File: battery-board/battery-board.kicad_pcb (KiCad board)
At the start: 2 copper layers, 101.6 x 14 mm, 6 parts, among them J1 Conn_01x02_Male, J2 Conn_01x03, J3 Screw_Terminal_01x01, SW1 RESET

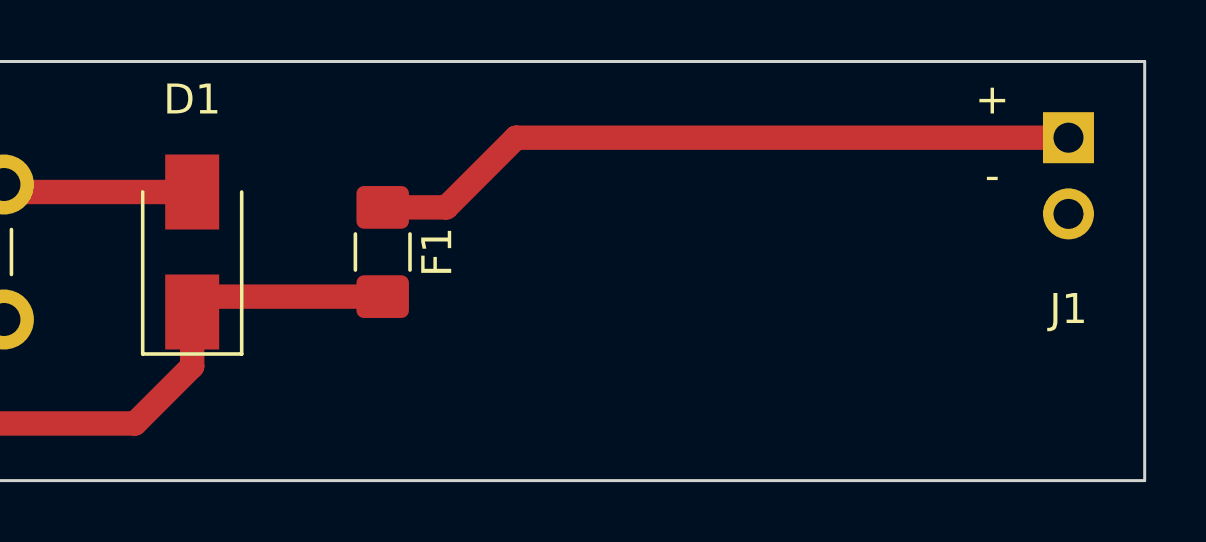
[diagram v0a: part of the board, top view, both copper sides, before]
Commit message: updated to a different fuse
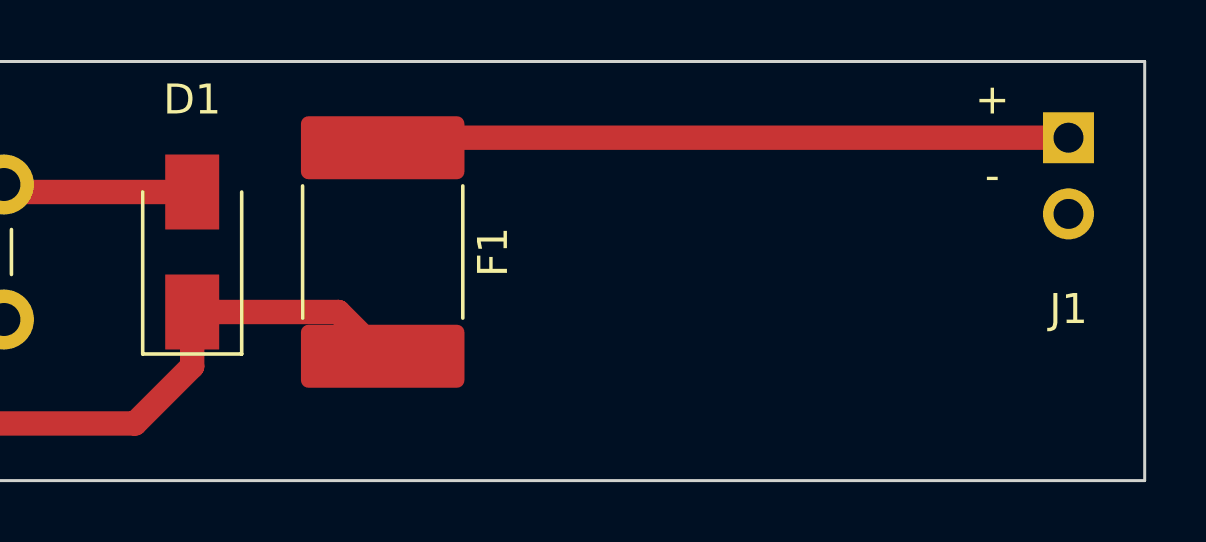
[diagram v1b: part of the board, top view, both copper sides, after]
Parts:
- F1: footprint Fuse:Fuse_1206_3216Metric_Pad1.42x1.75mm_HandSolder -> project:Fuse_2920_7451Metric_Pad2.10x5.45mm_HandSolder
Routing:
- net /VBB: track 23.8 -> 23.0 mm
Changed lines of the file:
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@@
 		)
 	)
-	(footprint "Fuse:Fuse_1206_3216Metric_Pad1.42x1.75mm_HandSolder"
+	(footprint "project:Fuse_2920_7451Metric_Pad2.10x5.45mm_HandSolder"
 		(layer "F.Cu")
 		(at 165.1 101.6 -90)
-		(descr "Fuse SMD 1206 (3216 Metric), square (rectangular) end terminal, IPC_7351 nominal with elongated pad for handsoldering. (Body size source: http://www.tortai-tech.com/upload/download/2011102023233369053.pdf), generated with kicad-footprint-generator")
+		(descr "Fuse SMD 2920 (7451 Metric), square (rectangular) end terminal, IPC_7351 nominal with elongated pad for handsoldering. (Body size from: http://www.megastar.com/products/fusetronic/polyswitch/PDF/smd2920.pdf), generated with kicad-footprint-generator")
 		(tags "fuse handsolder")
 		(property "Reference" "F1"
-			(at 0 -1.82 270)
+			(at 0 -3.68 270)
 			(layer "F.SilkS")
 			(effects
@@
 		)
 		(property "Value" "0.5A"
-			(at 0 1.82 270)
+			(at 0 3.68 270)
 			(layer "F.Fab")
 			(effects
@@
 		(attr smd)
 		(fp_line
-			(start -0.602064 0.91)
-			(end 0.602064 0.91)
+			(start -2.203752 2.67)
+			(end 2.203752 2.67)
 			(stroke
 				(width 0.12)
@@
 		)
 		(fp_line
-			(start -0.602064 -0.91)
-			(end 0.602064 -0.91)
+			(start -2.203752 -2.67)
+			(end 2.203752 -2.67)
 			(stroke
 				(width 0.12)
@@
 		)
 		(fp_line
-			(start -2.45 1.12)
-			(end -2.45 -1.12)
+			(start -4.78 2.98)
+			(end -4.78 -2.98)
 			(stroke
 				(width 0.05)
@@
 		)
 		(fp_line
-			(start 2.45 1.12)
-			(end -2.45 1.12)
+			(start 4.78 2.98)
+			(end -4.78 2.98)
 			(stroke
 				(width 0.05)
@@
 		)
 		(fp_line
-			(start -2.45 -1.12)
-			(end 2.45 -1.12)
+			(start -4.78 -2.98)
+			(end 4.78 -2.98)
 			(stroke
 				(width 0.05)
@@
 		)
 		(fp_line
-			(start 2.45 -1.12)
-			(end 2.45 1.12)
+			(start 4.78 -2.98)
+			(end 4.78 2.98)
 			(stroke
 				(width 0.05)
@@
 		)
 		(fp_line
-			(start -1.6 0.8)
-			(end -1.6 -0.8)
-			(stroke
-				(width 0.1)
-				(type solid)
-			)
-			(layer "F.Fab")
-		)
-		(fp_line
-			(start 1.6 0.8)
-			(end -1.6 0.8)
-			(stroke
-				(width 0.1)
-				(type solid)
-			)
-			(layer "F.Fab")
-		)
-		(fp_line
-			(start -1.6 -0.8)
-			(end 1.6 -0.8)
-			(stroke
-				(width 0.1)
-				(type solid)
-			)
-			(layer "F.Fab")
-		)
-		(fp_line
-			(start 1.6 -0.8)
-			(end 1.6 0.8)
+			(start -3.6775 2.56)
+			(end -3.6775 -2.56)
+			(stroke
+				(width 0.1)
+				(type solid)
+			)
+			(layer "F.Fab")
+		)
+		(fp_line
+			(start 3.6775 2.56)
+			(end -3.6775 2.56)
+			(stroke
+				(width 0.1)
+				(type solid)
+			)
+			(layer "F.Fab")
+		)
+		(fp_line
+			(start -3.6775 -2.56)
+			(end 3.6775 -2.56)
+			(stroke
+				(width 0.1)
+				(type solid)
+			)
+			(layer "F.Fab")
+		)
+		(fp_line
+			(start 3.6775 -2.56)
+			(end 3.6775 2.56)
 			(stroke
 				(width 0.1)
@@
 			(effects
 				(font
-					(size 0.8 0.8)
-					(thickness 0.12)
+					(size 1 1)
+					(thickness 0.15)
 				)
 			)
 		)
 		(pad "1" smd roundrect
-			(at -1.4875 0 270)
-			(size 1.425 1.75)
+			(at -3.475 0 270)
+			(size 2.1 5.45)
 			(layers "F.Cu" "F.Mask" "F.Paste")
-			(roundrect_rratio 0.175439)
+			(roundrect_rratio 0.119048)
 			(net 3 "/VBB")
 			(pintype "passive")
 		)
 		(pad "2" smd roundrect
-			(at 1.4875 0 270)
-			(size 1.425 1.75)
+			(at 3.475 0 270)
+			(size 2.1 5.45)
 			(layers "F.Cu" "F.Mask" "F.Paste")
-			(roundrect_rratio 0.175439)
+			(roundrect_rratio 0.119048)
 			(net 1 "/VCC")
 			(pintype "passive")
 		)
 		(embedded_fonts no)
-		(model "${KICAD8_3DMODEL_DIR}/Fuse.3dshapes/Fuse_1206_3216Metric.wrl"
+		(model "${KIPRJMOD}/project.pretty/mf-lsmf050x.stp"
 			(offset
-				(xyz 0 0 0)
+				(xyz -3.75 2.6 0)
 			)
 			(scale
@@
 			)
 			(rotate
-				(xyz 0 0 0)
+				(xyz 90 -0 -0)
 			)
 		)
@@
 	)
 	(segment
-		(start 159.2625 103.0875)
+		(start 163.625 103.6)
 		(end 158.75 103.6)
+		(width 0.8128)
+		(layer "F.Cu")
+		(net 1)
+	)
+	(segment
+		(start 165.1 105.075)
+		(end 163.625 103.6)
 		(width 0.8128)
 		(layer "F.Cu")
@@
 	)
 	(segment
-		(start 165.1 103.0875)
-		(end 159.2625 103.0875)
-		(width 0.8128)
-		(layer "F.Cu")
-		(net 1)
-	)
-	(segment
 		(start 158.75 103.6)
 		(end 158.75 105.41)
@@
 	(segment
 		(start 187.96 97.79)
-		(end 169.545 97.79)
+		(end 165.435 97.79)
 		(width 0.8128)
 		(layer "F.Cu")
@@
 	)
 	(segment
-		(start 169.545 97.79)
-		(end 167.2225 100.1125)
-		(width 0.8128)
-		(layer "F.Cu")
-		(net 3)
-	)
-	(segment
-		(start 167.2225 100.1125)
-		(end 165.1 100.1125)
-		(width 0.8128)
-		(layer "F.Cu")
+		(start 165.435 97.79)
+		(end 165.1 98.125)
+		(width 0.8128)
+		(layer "F.Cu")
